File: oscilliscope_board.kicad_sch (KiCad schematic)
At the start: 8 parts, among them J1 Conn_Coaxial, J2 Conn_Coaxial, SW1 SW_Push, U2 ADC0832

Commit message: schematic capture complete
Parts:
- added C1, C2, C3: 10uF, symbol Device:C_Polarized
- added U3: ~, symbol Arduino:TFT_LCD_ArduinoMegaShield
- U2: footprint (none) -> Package_DIP:CERDIP-8_W7.62mm_SideBrazed
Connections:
- net +5V: now also U1.24 (VU), C1.1, C2.1, C3.1, U3.1 (5V), U3.2 (5V)
- net GNDD: now also U1.25 (GND), C1.2, C2.2, C3.2, U3.35 (GND), U3.36 (GND)
- net at U1.29 (PIO29): now also U3.3 (DB8)
- net at U1.30 (PIO30): now also U3.4 (DB9)
- net at U1.31 (PIO31): now also U3.5 (DB10)
- net at U1.32 (PIO32): now also U3.6 (DB11)
- net at U1.33 (PIO33): now also U3.7 (DB12)
- net at U1.34 (PIO34): now also U3.8 (DB13)
- net at U1.35 (PIO35): now also U3.9 (DB14)
- net at U1.36 (PIO36): now also U3.10 (DB15)
- net at U1.37 (PIO37): now also U3.11 (DB7)
- net at U1.38 (PIO38): now also U3.12 (DB6)
- net at U1.39 (PIO39): now also U3.13 (DB5)
- net at U1.40 (PIO40): now also U3.14 (DB4)
- net at U1.41 (PIO41): now also U3.15 (DB3)
- net at U1.42 (PIO42): now also U3.16 (DB2)
- net at U1.43 (PIO43): now also U3.17 (DB1)
- net at U1.44 (PIO44): now also U3.18 (DB0)
- net at U1.45 (PIO45): now also U3.19 (RS)
- net at U1.46 (PIO46): now also U3.20 (WR)
- net at U1.47 (PIO47): now also U3.21 (CS)
- net at U1.48 (PIO48): now also U3.22 (RST)
- no-connect marks 0 -> 26
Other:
- note added: "TFT LCD Module"
- moved on the sheet: J1, J2, R1, R2, R3, SW1, U1, U2

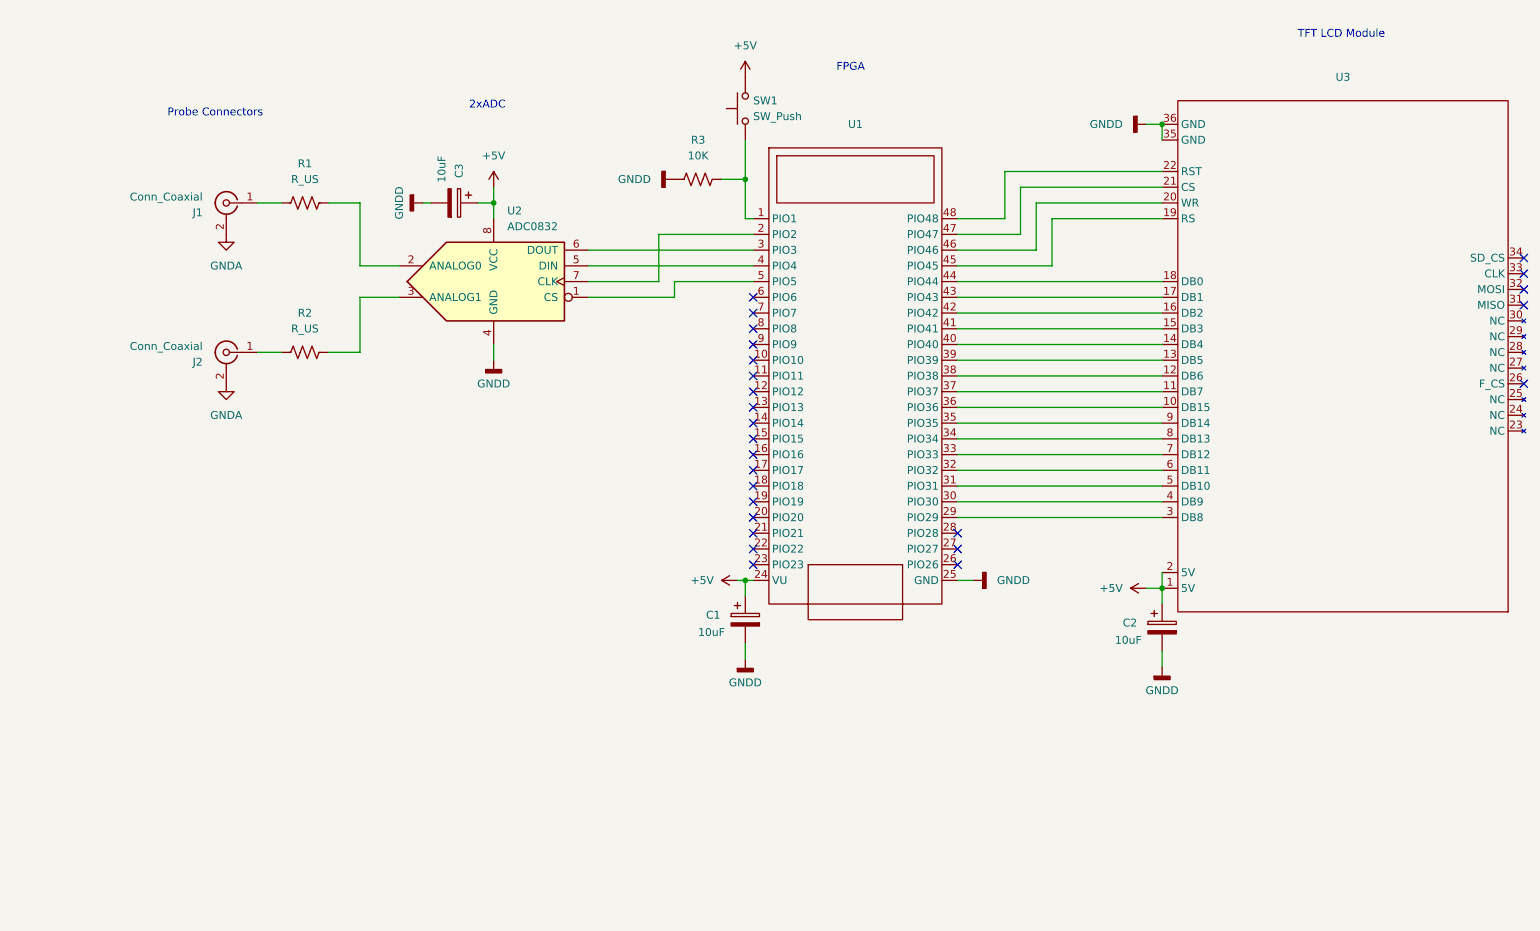
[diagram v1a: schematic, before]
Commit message: new footprints for lcd shield and Xilinx fpga, assigned foorprints
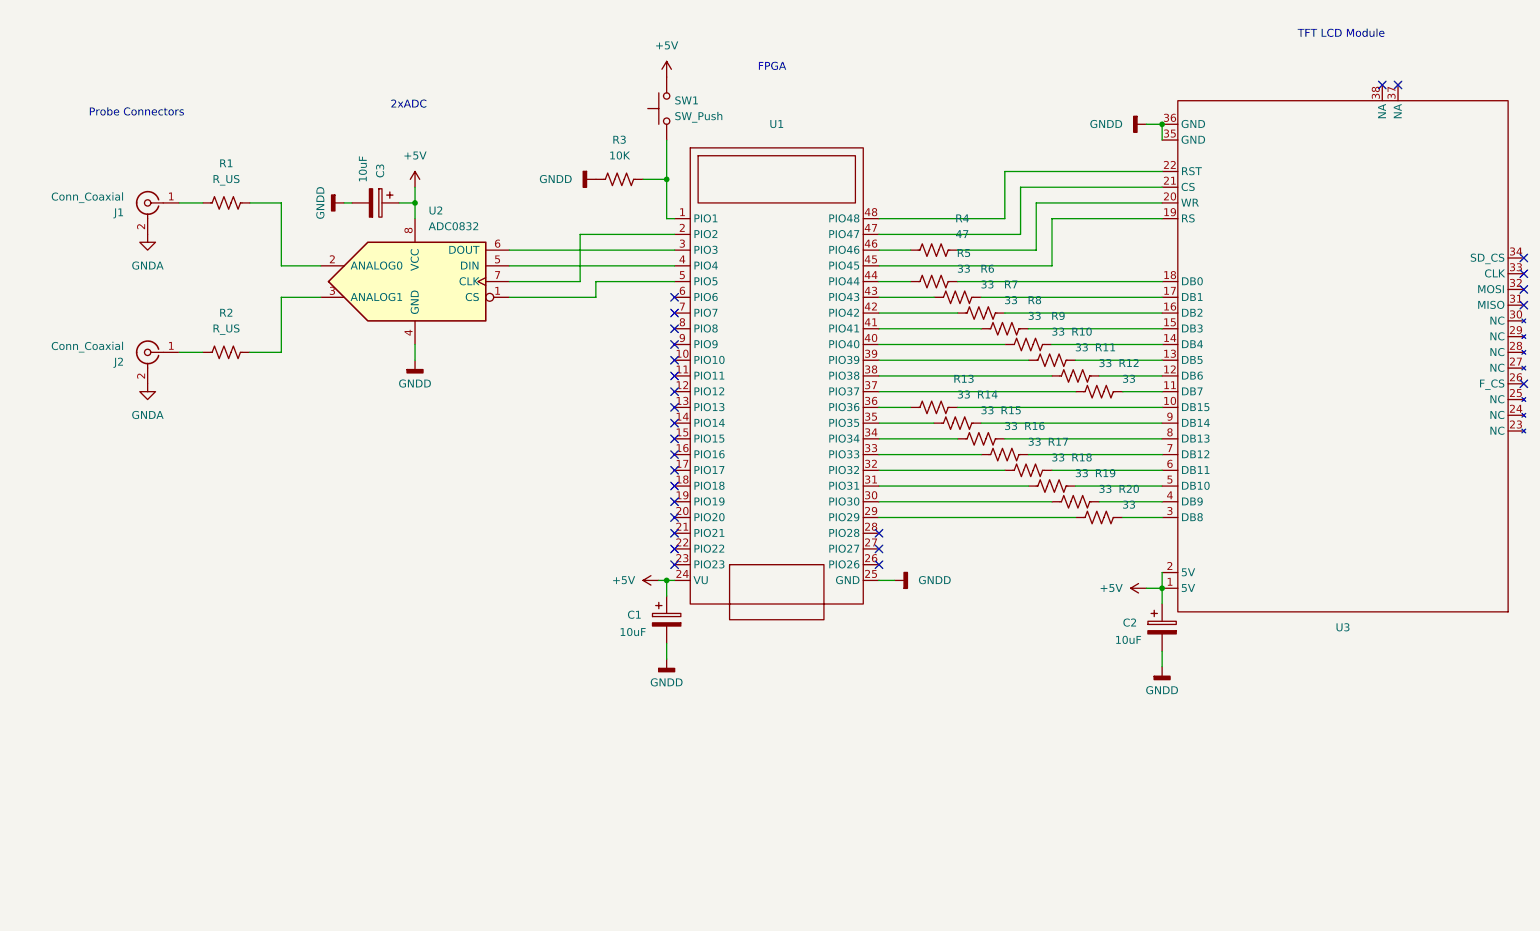
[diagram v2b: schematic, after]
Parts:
- added R10, R11, R12, R13, R14, R15, R16, R17, R18, R19, R20, R5, R6, R7, R8, R9: 33, Resistor_SMD:R_1206_3216Metric_Pad1.30x1.75mm_HandSolder, symbol Device:R_US
- added R4: 47, Resistor_SMD:R_1206_3216Metric_Pad1.30x1.75mm_HandSolder, symbol Device:R_US
- C1, C2, C3: footprint (none) -> Capacitor_THT:CP_Radial_D8.0mm_P5.00mm
- R1, R2: footprint (none) -> Resistor_SMD:R_1206_3216Metric_Pad1.30x1.75mm_HandSolder
- R3: footprint (none) -> Resistor_THT:R_Axial_DIN0204_L3.6mm_D1.6mm_P7.62mm_Horizontal
- SW1: footprint (none) -> Button_Switch_Keyboard:SW_Cherry_MX_1.00u_Plate
- U1: footprint (none) -> oscilloscope:Cmod A7 35T CPG236
- U3: footprint (none) -> oscilloscope:TFT LCD 3.5 ArduinoMega Shield
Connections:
- net at U1.36 (PIO36): now also R13.1; no longer U3.10 (DB15)
- net at U3.11 (DB7): now also R12.2; no longer U1.37 (PIO37)
- net at U1.38 (PIO38): now also R11.1; no longer U3.12 (DB6)
- net at U1.39 (PIO39): now also R10.1; no longer U3.13 (DB5)
- net at U3.14 (DB4): now also R9.2; no longer U1.40 (PIO40)
- net at U1.41 (PIO41): now also R8.1; no longer U3.15 (DB3)
- net at U3.16 (DB2): now also R7.2; no longer U1.42 (PIO42)
- net at U1.43 (PIO43): now also R6.1; no longer U3.17 (DB1)
- net at U1.44 (PIO44): now also R5.1; no longer U3.18 (DB0)
- net at U3.20 (WR): now also R4.2; no longer U1.46 (PIO46)
- net at U3.3 (DB8): now also R20.2; no longer U1.29 (PIO29)
- net at U1.30 (PIO30): now also R19.1; no longer U3.4 (DB9)
- net at U1.31 (PIO31): now also R18.1; no longer U3.5 (DB10)
- net at U1.32 (PIO32): now also R17.1; no longer U3.6 (DB11)
- net at U3.7 (DB12): now also R16.2; no longer U1.33 (PIO33)
- net at U1.34 (PIO34): now also R15.1; no longer U3.8 (DB13)
- net at U3.9 (DB14): now also R14.2; no longer U1.35 (PIO35)
- new net: R10.2, U3.13 (DB5)
- new net: R5.2, U3.18 (DB0)
- new net: R17.2, U3.6 (DB11)
- new net: R15.2, U3.8 (DB13)
- new net: R13.2, U3.10 (DB15)
- new net: R11.2, U3.12 (DB6)
- new net: R18.2, U3.5 (DB10)
- new net: R6.2, U3.17 (DB1)
- new net: R8.2, U3.15 (DB3)
- new net: R19.2, U3.4 (DB9)
- new net: R4.1, U1.46 (PIO46)
- new net: R20.1, U1.29 (PIO29)
- new net: R16.1, U1.33 (PIO33)
- new net: R14.1, U1.35 (PIO35)
- new net: R12.1, U1.37 (PIO37)
- new net: R9.1, U1.40 (PIO40)
- new net: R7.1, U1.42 (PIO42)
- no-connect marks 26 -> 28
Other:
- moved on the sheet: C1, C3, J1, J2, R1, R2, R3, SW1, U1, U2

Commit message: new footprint from digikey
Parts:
- J1, J2: footprint (none) -> oscilloscope:LINX_CONBNC001
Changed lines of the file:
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@@
 			)
 		)
-		(property "Footprint" ""
+		(property "Footprint" "oscilloscope:LINX_CONBNC001"
 			(at 39.37 95.25 0)
 			(effects
@@
 			)
 		)
-		(property "Footprint" ""
+		(property "Footprint" "oscilloscope:LINX_CONBNC001"
 			(at 39.37 71.12 0)
 			(effects

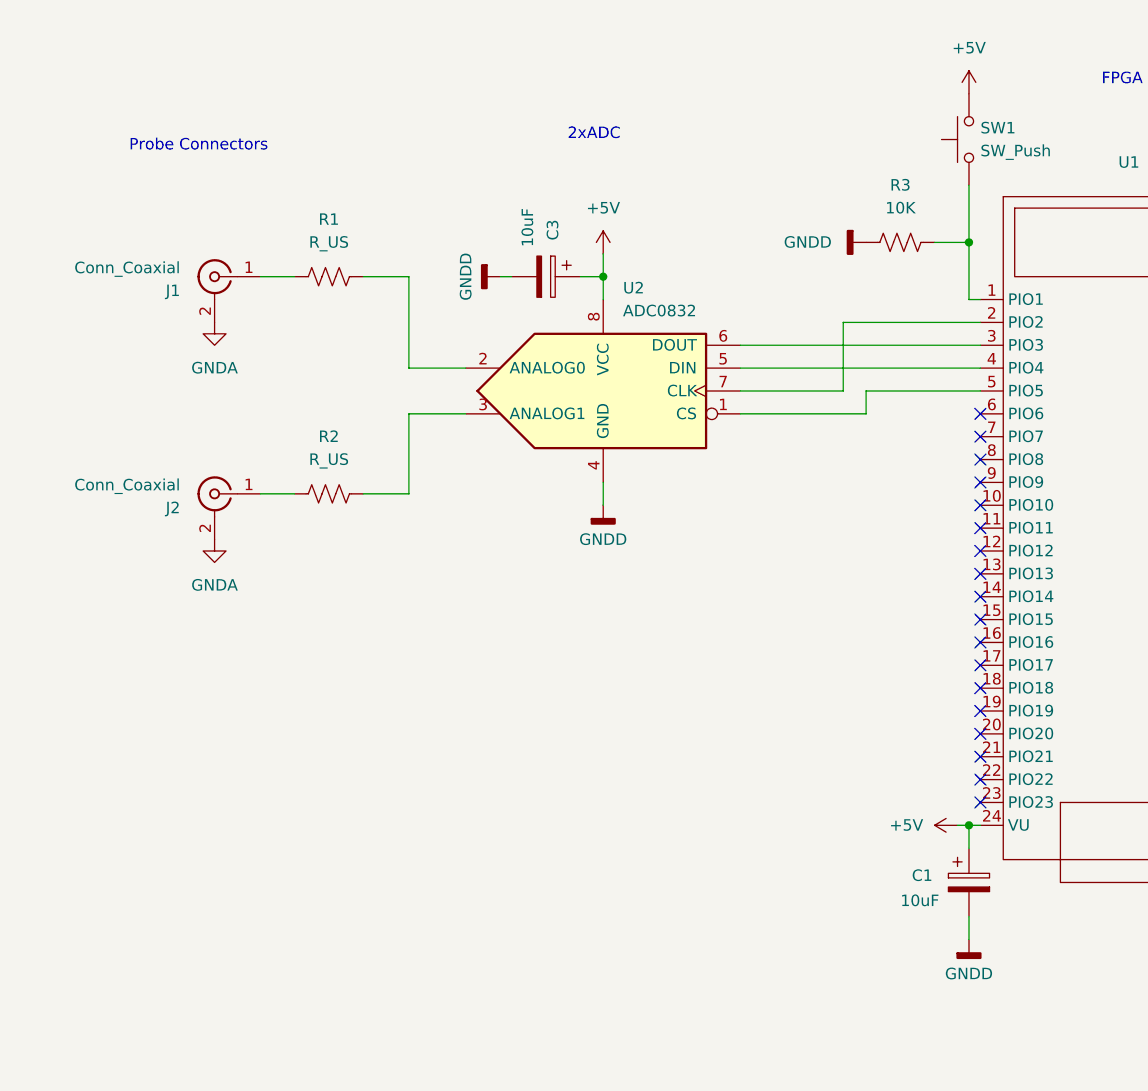
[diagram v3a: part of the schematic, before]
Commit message: added rotary encoder to schematic
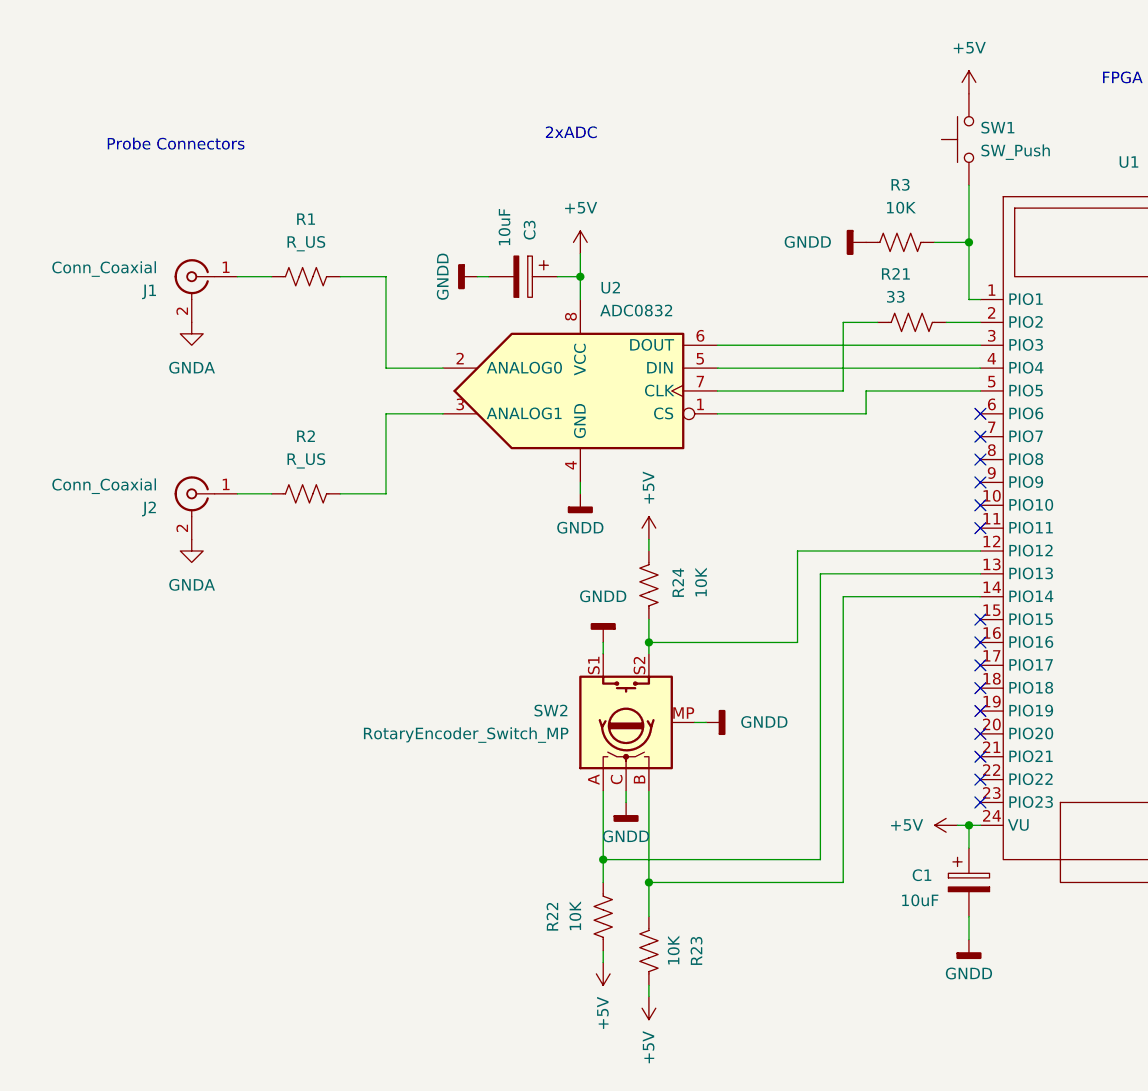
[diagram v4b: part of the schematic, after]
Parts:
- added R21: 33, Resistor_SMD:R_1206_3216Metric_Pad1.30x1.75mm_HandSolder, symbol Device:R_US
- added R22, R23, R24: 10K, symbol Device:R_US
- added SW2: RotaryEncoder_Switch_MP, symbol Device:RotaryEncoder_Switch_MP
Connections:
- net +5V: now also R22.1, R23.1, R24.1
- net GNDD: now also SW2.C, SW2.MP, SW2.S1
- net at U2.7 (CLK): now also R21.1; no longer U1.2 (PIO2)
- net at U1.12 (PIO12): now also R24.2, SW2.S2
- net at U1.13 (PIO13): now also R22.2, SW2.A
- net at U1.14 (PIO14): now also R23.2, SW2.B
- new net: R21.2, U1.2 (PIO2)
- no-connect marks 28 -> 25
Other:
- moved on the sheet: C3, J1, J2, R1, R2, U2

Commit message: assigned footprint
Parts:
- SW2: footprint (none) -> Rotary_Encoder:RotaryEncoder_Bourns_Vertical_PEC12R-3x17F-Sxxxx
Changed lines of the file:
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@@
 			)
 		)
-		(property "Footprint" ""
+		(property "Footprint" "Rotary_Encoder:RotaryEncoder_Bourns_Vertical_PEC12R-3x17F-Sxxxx"
 			(at 81.026 124.46 0)
 			(effects

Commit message: new pcb file, all footprints assigned. ready to start layout
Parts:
- R22, R23, R24: footprint (none) -> Resistor_SMD:R_1206_3216Metric_Pad1.30x1.75mm_HandSolder
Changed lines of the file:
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@@
 			)
 		)
-		(property "Footprint" ""
+		(property "Footprint" "Resistor_SMD:R_1206_3216Metric_Pad1.30x1.75mm_HandSolder"
 			(at 86.614 105.664 90)
 			(effects
@@
 			)
 		)
-		(property "Footprint" ""
+		(property "Footprint" "Resistor_SMD:R_1206_3216Metric_Pad1.30x1.75mm_HandSolder"
 			(at 88.646 145.796 90)
 			(effects
@@
 			)
 		)
-		(property "Footprint" ""
+		(property "Footprint" "Resistor_SMD:R_1206_3216Metric_Pad1.30x1.75mm_HandSolder"
 			(at 81.534 141.986 90)
 			(effects
